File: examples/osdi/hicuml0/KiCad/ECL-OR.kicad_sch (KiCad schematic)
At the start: 16 parts, among them Q1 NP, Q2 NP, Q3 NP, Q4 NP, Q5 NP

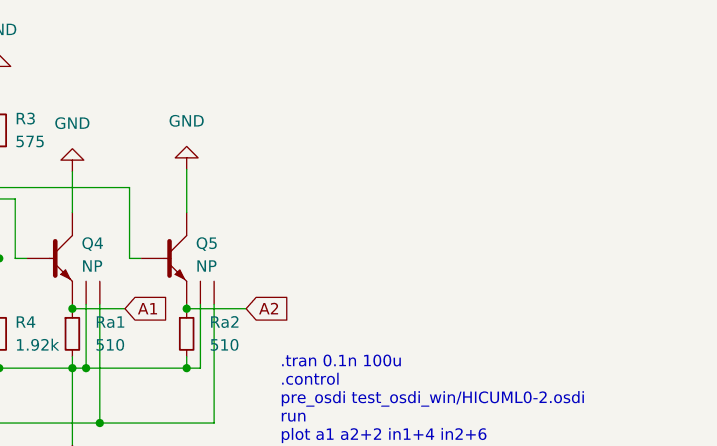
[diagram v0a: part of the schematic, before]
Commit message: Rename examples for ECL OR gate Simulate OR gate faster TSTEP 0.1n -> 0.3n
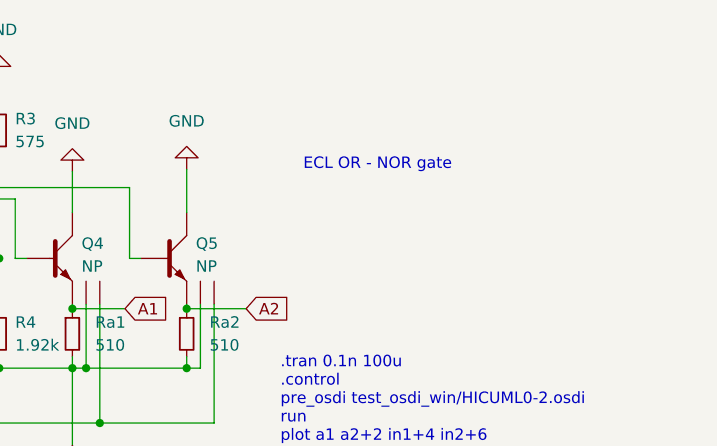
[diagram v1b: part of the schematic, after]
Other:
- note added: "ECL OR - NOR gate"
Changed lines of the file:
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@@
     (stroke (width 0) (type default) (color 0 0 0 0))
+  )
+  (text "ECL OR - NOR gate" (at 245.364 87.884 0)
+    (effects (font (size 1.27 1.27)) (justify left bottom))
   )
   (text ".tran 0.1n 100u\n.control\npre_osdi test_osdi_win/HICUML0-2.osdi\nrun\nplot a1 a2+2 in1+4 in2+6\n.endc"

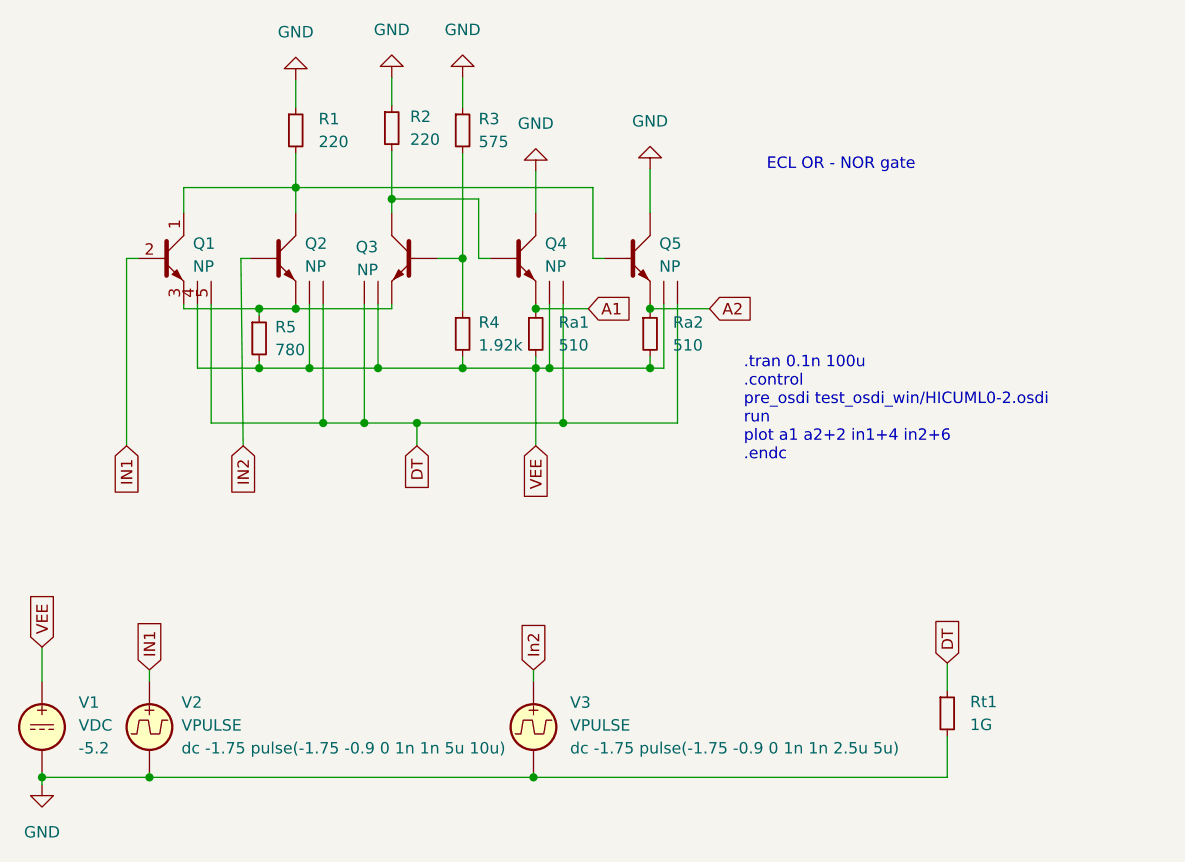
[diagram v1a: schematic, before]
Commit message: Rename projetc to OR (OR-gate) Add new path (absolute, so has to be modified by any user)
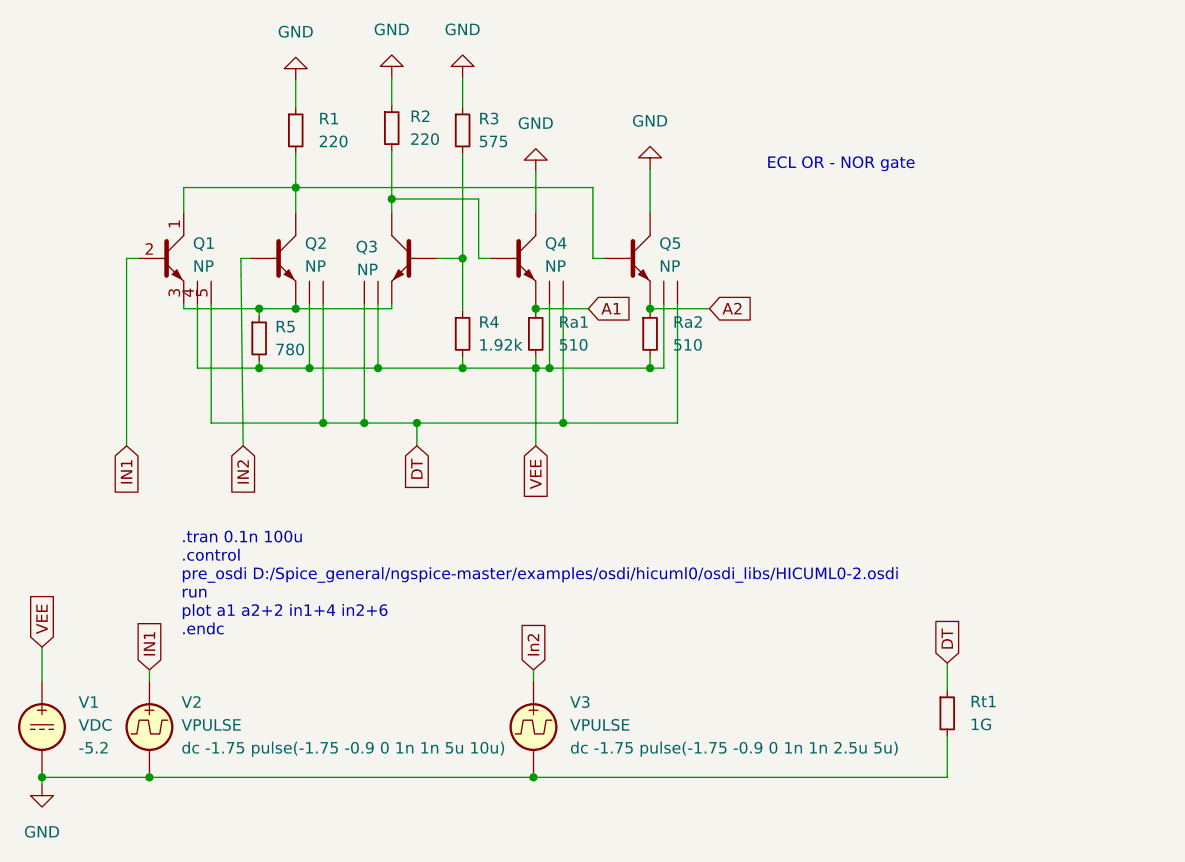
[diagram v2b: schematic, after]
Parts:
- Q1, Q2, Q3, Q4, Q5: Spice_Lib_File model-card-hicumL0V1p11_mod.lib -> D:\Spice_general\ngspice-master\examples\osdi\hicuml0\Model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
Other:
- note added: ".tran 0.1n 100u .control pre_osdi D:/Spice_general/ngspice-master/examples/osdi/hicuml0/osdi_libs/HICUML0-2.osdi run plot a1 a2+2 in1+4 in2+6 .endc"
- note removed: ".tran 0.1n 100u .control pre_osdi test_osdi_win/HICUML0-2.osdi run plot a1 a2+2 in1+4 in2+6 .endc"
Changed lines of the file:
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@@
     (effects (font (size 1.27 1.27)) (justify left bottom))
   )
-  (text ".tran 0.1n 100u\n.control\npre_osdi test_osdi_win/HICUML0-2.osdi\nrun\nplot a1 a2+2 in1+4 in2+6\n.endc"
-    (at 242.824 120.142 0)
+  (text ".tran 0.1n 100u\n.control\npre_osdi D:/Spice_general/ngspice-master/examples/osdi/hicuml0/osdi_libs/HICUML0-2.osdi\nrun\nplot a1 a2+2 in1+4 in2+6\n.endc"
+    (at 180.34 139.7 0)
     (effects (font (size 1.27 1.27)) (justify left bottom))
   )
@@
       (effects (font (size 1.27 1.27)) hide)
     )
-    (property "Spice_Lib_File" "model-card-hicumL0V1p11_mod.lib" (id 7) (at 187.96 97.536 0)
+    (property "Spice_Lib_File" "D:\\Spice_general\\ngspice-master\\examples\\osdi\\hicuml0\\Modelcards\\model-card-hicumL0V1p11_mod.lib" (id 7) (at 187.96 97.536 0)
       (effects (font (size 1.27 1.27)) hide)
     )
@@
       (effects (font (size 1.27 1.27)) hide)
     )
-    (property "Spice_Lib_File" "model-card-hicumL0V1p11_mod.lib" (id 7) (at 208.788 97.536 0)
+    (property "Spice_Lib_File" "D:\\Spice_general\\ngspice-master\\examples\\osdi\\hicuml0\\Modelcards\\model-card-hicumL0V1p11_mod.lib" (id 7) (at 208.788 97.536 0)
       (effects (font (size 1.27 1.27)) hide)
     )
@@
       (effects (font (size 1.27 1.27)) hide)
     )
-    (property "Spice_Lib_File" "model-card-hicumL0V1p11_mod.lib" (id 7) (at 227.33 97.536 0)
+    (property "Spice_Lib_File" "D:\\Spice_general\\ngspice-master\\examples\\osdi\\hicuml0\\Modelcards\\model-card-hicumL0V1p11_mod.lib" (id 7) (at 227.33 97.536 0)
       (effects (font (size 1.27 1.27)) hide)
     )
@@
       (effects (font (size 1.27 1.27)) hide)
     )
-    (property "Spice_Lib_File" "model-card-hicumL0V1p11_mod.lib" (id 7) (at 175.514 97.536 0)
+    (property "Spice_Lib_File" "D:\\Spice_general\\ngspice-master\\examples\\osdi\\hicuml0\\Modelcards\\model-card-hicumL0V1p11_mod.lib" (id 7) (at 175.514 97.536 0)
       (effects (font (size 1.27 1.27)) hide)
     )
@@
       (effects (font (size 1.27 1.27)) hide)
     )
-    (property "Spice_Lib_File" "model-card-hicumL0V1p11_mod.lib" (id 7) (at 214.63 97.536 0)
-      (effects (font (size 1.27 1.27)) hide)
-    )
+    (property "Spice_Lib_File" "D:\\Spice_general\\ngspice-master\\examples\\osdi\\hicuml0\\Modelcards\\model-card-hicumL0V1p11_mod.lib" (id 7) (at 214.63 97.536 0)
+      (effects (font (size 1.27 1.27)) hide)
+    )
